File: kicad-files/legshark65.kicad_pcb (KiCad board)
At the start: 2 copper layers, 286 x 96 mm, 158 parts, among them J1 ARM JTAG, SW1 K2-1187SQ-A4SW-06, SW2 PCM12SMTR, T2 53261-0471, U1 STM32F411CEU6, U3 AT24C256C-SSHL-T, Y1 TAXM8M4RFDCET2T

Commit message: More minor clearance changes
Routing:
- net c13: track 92.9 -> 94.6 mm
- net 3V3: track 119.6 -> 120.5 mm
- net c0: track 312.5 -> 313.2 mm

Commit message: Added some front graphics to the motherboard pcb
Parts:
- removed Legshark_Logo2: Huge, Legshark:Legshark_Logo_Huge
- added H1: JM Logo, Legshark:jm_logo, F.Cu at (259.6, 112.8)
- added H2: LS65 Logo, Legshark:ls65_logo, F.Cu at (293.8, 113.2)
- added H3: LS Logo, Legshark:Legshark_Mask, F.Cu at (251.1, 112.9)
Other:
- board text added: "Legshark65 version 1.0 Ortholinear keyboard"
- board text added: "Made by Jemmec"

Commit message: Finished add BOM to motherboard & fixing some small parts
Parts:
- added J2: Conn_01x04, acheron_Connectors:PinHeader_1x4_P2.54mm_Vertical, F.Cu at (208.6, 80.3)
- added R2: 0R, Resistor_SMD:R_0603_1608Metric, B.Cu at (223.4, 81.1)
- added R3: 0R, Resistor_SMD:R_0603_1608Metric, B.Cu at (223.4, 79.6)
- C16: value 16V 10uF Tantallum -> 10u
- U3: footprint acheron_Components:TSSOP-8_4.4x3mm_P0.65mm -> acheron_Components:SOIC-8
- moved U3 0.32 mm to (265.9, 62.1)
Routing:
- net 3V3: track 120.5 -> 143.7 mm
- net Net-(J2-Pin_3): track 0.00 -> 14.2 mm
- net Net-(J2-Pin_2): track 0.00 -> 14.2 mm
- net D+: track 25.2 -> 31.5 mm
- net D-: track 25.2 -> 31.5 mm
- net GND: track 23.5 -> 21.8 mm, vias 20 -> 21
- net c12: track 78.5 -> 77.7 mm
- net SWCLK: track 50.7 -> 50.2 mm
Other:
- board text added: "Hardwire"
- board text added: "Molex PicoBlade"

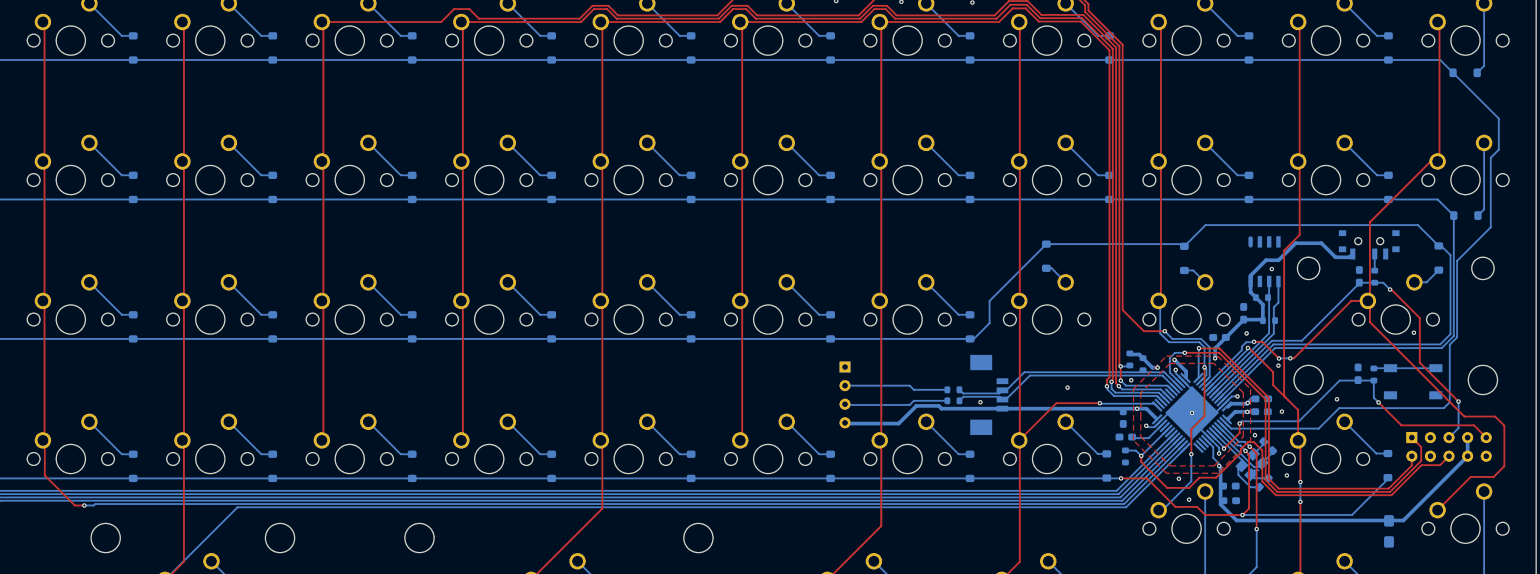
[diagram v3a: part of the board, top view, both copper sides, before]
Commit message: Lots of small routing and quality changes to the motherboard
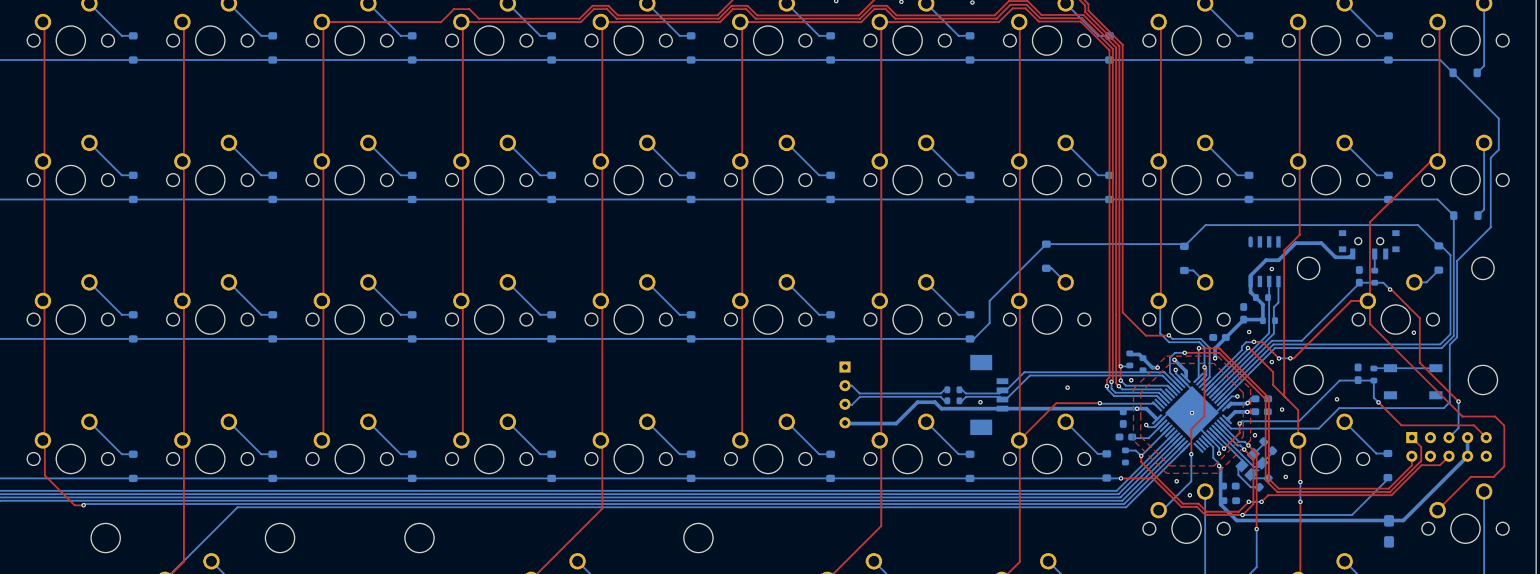
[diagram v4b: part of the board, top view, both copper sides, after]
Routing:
- net BOOT1: track 62.5 -> 56.4 mm, vias 1 -> 3
- net c14: track 118.3 -> 116.2 mm
- net r3: track 256.5 -> 257.0 mm

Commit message: Made the board's edge cut slightly smaller
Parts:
- moved H2 2.77 mm to (291.0, 113.2)
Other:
- board size 286 x 96 mm -> 282 x 94 mm
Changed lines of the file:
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@@
   )
   (footprint "Legshark:ls65_logo" (layer "F.Cu")
-    (at 293.765519 113.174295)
+    (at 291 113.174295)
     (property "Sheetfile" "legshark65.kicad_sch")
     (property "Sheetname" "")
@@
   (gr_line (start 47.5 116.25) (end 47.5 112.25)
     (stroke (width 0.4) (type default)) (layer "F.SilkS"))
-  (gr_line (start 17 116) (end 17 24)
+  (gr_line (start 19 115) (end 19 25)
     (stroke (width 0.1) (type default)) (layer "Edge.Cuts"))
-  (gr_arc (start 301 22) (mid 302.414214 22.585786) (end 303 24)
+  (gr_arc (start 299 23) (mid 300.414214 23.585786) (end 301 25)
     (stroke (width 0.1) (type default)) (layer "Edge.Cuts"))
-  (gr_arc (start 17 24) (mid 17.585786 22.585786) (end 19 22)
+  (gr_arc (start 19 25) (mid 19.585786 23.585786) (end 21 23)
     (stroke (width 0.1) (type default)) (layer "Edge.Cuts"))
-  (gr_arc (start 19 118) (mid 17.585786 117.414214) (end 17 116)
+  (gr_arc (start 21 117) (mid 19.585786 116.414214) (end 19 115)
     (stroke (width 0.1) (type default)) (layer "Edge.Cuts"))
-  (gr_arc (start 303 116) (mid 302.414214 117.414214) (end 301 118)
+  (gr_arc (start 301 115) (mid 300.414214 116.414214) (end 299 117)
     (stroke (width 0.1) (type default)) (layer "Edge.Cuts"))
-  (gr_line (start 301 118) (end 19 118)
+  (gr_line (start 299 117) (end 21 117)
     (stroke (width 0.1) (type default)) (layer "Edge.Cuts"))
-  (gr_line (start 19 22) (end 301 22)
+  (gr_line (start 21 23) (end 299 23)
     (stroke (width 0.1) (type default)) (layer "Edge.Cuts"))
-  (gr_line (start 303 24) (end 303 116)
+  (gr_line (start 301 25) (end 301 115)
     (stroke (width 0.1) (type default)) (layer "Edge.Cuts"))
   (gr_text "2.25u" (at 107.5 107.2) (layer "B.SilkS")
@@
     (connect_pads (clearance 0.2))
     (min_thickness 0.25) (filled_areas_thickness no)
-    (fill yes (thermal_gap 0.2) (thermal_bridge_width 0.25) (island_removal_mode 1) (island_area_min 10))
+    (fill (thermal_gap 0.2) (thermal_bridge_width 0.25) (island_removal_mode 1) (island_area_min 10))
     (polygon
       (pts
@@
     (connect_pads (clearance 0.2))
     (min_thickness 0.2) (filled_areas_thickness no)
-    (fill yes (thermal_gap 0.25) (thermal_bridge_width 0.25) (smoothing fillet) (radius 1))
+    (fill (thermal_gap 0.25) (thermal_bridge_width 0.25) (smoothing fillet) (radius 1))
     (polygon
       (pts
